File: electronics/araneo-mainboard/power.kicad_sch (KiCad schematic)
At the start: 1 part, among them IC3 TPS54302DDCR

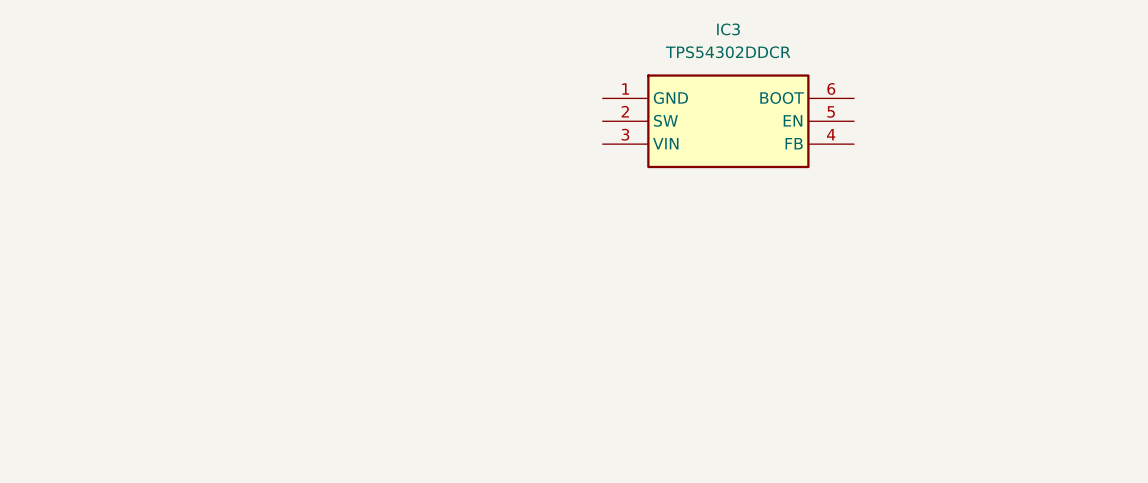
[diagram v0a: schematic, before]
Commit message: add components schematics
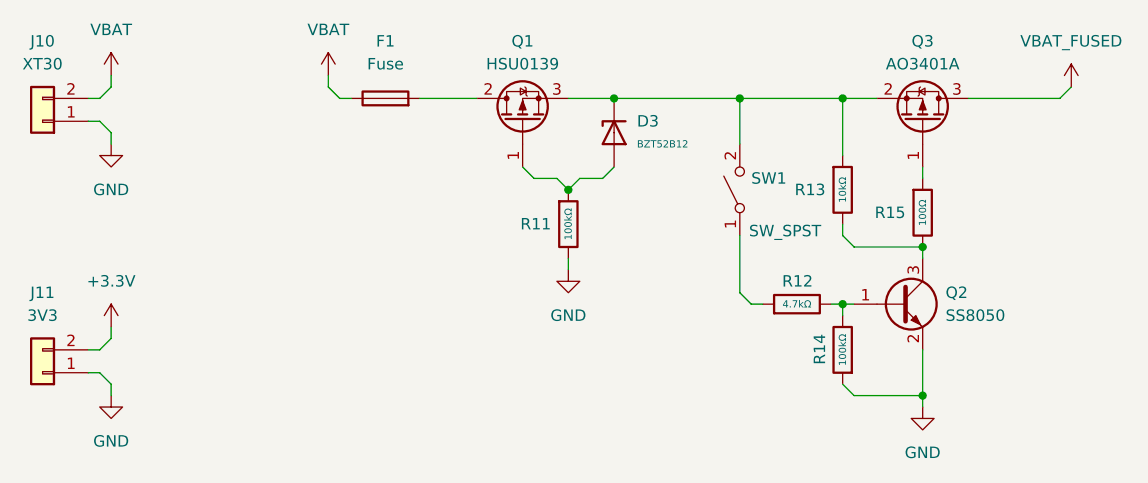
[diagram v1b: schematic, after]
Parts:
- removed IC3: TPS54302DDCR, SOT95P280X110-6N, symbol Symbols:TPS54302DDCR
- added D3: BZT52B12, PCM_JLCPCB:D_SOD-123, symbol PCM_JLCPCB-Diodes:Zener,BZT52B12
- added F1: Fuse, PCM_SparkFun-Fuse:Fuseholder_Automotive, symbol Device:Fuse
- added J10: XT30, Connector_AMASS:AMASS_XT30U-F_1x02_P5.0mm_Vertical, symbol Connector_Generic:Conn_01x02
- added J11: 3V3, Connector_PinHeader_2.54mm:PinHeader_1x02_P2.54mm_Vertical, symbol Connector_Generic:Conn_01x02
- added Q1: HSU0139, HSU0139:HSU0139, symbol Symbols:HSU0139
- added Q2: SS8050, Package_TO_SOT_SMD:SOT-23, symbol Transistor_BJT:SS8050
- added Q3: AO3401A, Package_TO_SOT_SMD:SOT-23, symbol Transistor_FET:AO3401A
- added R11, R14: 100kΩ, PCM_JLCPCB:R_0402, symbol PCM_JLCPCB-Resistors:0402,1.2kΩ
- added R12: 4.7kΩ, PCM_JLCPCB:R_0402, symbol PCM_JLCPCB-Resistors:0402,1.2kΩ
- added R13: 10kΩ, PCM_JLCPCB:R_0402, symbol PCM_JLCPCB-Resistors:0402,1.2kΩ
- added R15: 100Ω, PCM_JLCPCB:R_0402, symbol PCM_JLCPCB-Resistors:0402,1.2kΩ
- added SW1: SW_SPST, Button_Switch_THT:SW_NKK_GW12LJP, symbol Switch:SW_SPST
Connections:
- new net: Q3.1 (G), R15.1
- new net: D3.1, Q1.2 (S), Q1.3 (S), Q3.2 (S), R13.1, SW1.2 (B)
- new net: Q2.3 (C), R13.2, R15.2
- new net: Q2.1 (B), R12.2, R14.2
- new net: F1.2, Q1.2 (S)
- new net: D3.2, Q1.1 (G), R11.1
- new net: R12.1, SW1.1 (A)
- new net +3.3V: J11.2 (Pin_2)
- new net GND: J10.1 (Pin_1), J11.1 (Pin_1), Q2.2 (E), R11.2, R14.1
- new net VBAT: F1.1, J10.2 (Pin_2)
- new net VBAT_FUSED: Q3.3 (D)

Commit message: electronics: assign footprints
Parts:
- Q1: footprint HSU0139:HSU0139 -> Custom:HSU0139
- SW1: footprint Button_Switch_THT:SW_NKK_GW12LJP -> PCM_SparkFun-Connector:ScrewTerminal_1x02_P3.5mm_Blue
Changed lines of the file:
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@@
 			)
 		)
-		(property "Footprint" "Button_Switch_THT:SW_NKK_GW12LJP"
+		(property "Footprint" "PCM_SparkFun-Connector:ScrewTerminal_1x02_P3.5mm_Blue"
 			(at 146.05 72.39 0)
 			(hide yes)
@@
 			)
 		)
-		(property "Footprint" "HSU0139:HSU0139"
+		(property "Footprint" "Custom:HSU0139"
 			(at 123.825 59.69 0)
 			(hide yes)

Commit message: add first layout
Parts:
- removed Q1: HSU0139, Custom:HSU0139, symbol Symbols:HSU0139
- added Q4: DMP3056LSS-13, PCM_SparkFun-Semiconductor-Standard:SO-8, symbol Transistor_FET:AO3401A
- F1: footprint PCM_SparkFun-Fuse:Fuseholder_Automotive -> Custom:3568
- Q3: value AO3401A -> DMP3056LSS-13; footprint Package_TO_SOT_SMD:SOT-23 -> PCM_SparkFun-Semiconductor-Standard:SO-8
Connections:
- net VBAT_FUSED: now also Q3.5 (D), Q3.6 (D), Q3.7 (D), Q3.8 (D); no longer Q3.3 (D)
- net SW_1: now reaches Q3.1 (S)
- net SW_1: now also D3.1, Q3.2 (S), Q3.3 (S), R13.1, SW1.2 (B), Q4.1 (S), Q4.2 (S), Q4.3 (S); no longer R15.1
- net SW_C_R: now reaches Q2.3 (C), R13.2, R15.2
- net SW_B_PD: now reaches Q2.1 (B), R12.2, R14.2
- net VBAT_F: now reaches F1.2
- net VBAT_F: now also Q4.5 (D), Q4.6 (D), Q4.7 (D), Q4.8 (D)
- net POL_ZENER: now reaches D3.2, R11.1
- net POL_ZENER: now also Q4.4 (G)
- net SW_2: now reaches R12.1, SW1.1 (A)
- new net SW_G: Q3.4 (G), R15.1
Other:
- moved on the sheet: F1
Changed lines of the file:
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@@
 	(wire
 		(pts
-			(xy 110.49 62.23) (xy 116.84 62.23)
+			(xy 105.41 62.23) (xy 116.84 62.23)
 		)
 		(stroke
@@
 	(wire
 		(pts
-			(xy 100.33 60.96) (xy 101.6 62.23)
+			(xy 95.25 60.96) (xy 96.52 62.23)
 		)
 		(stroke
@@
 	(wire
 		(pts
-			(xy 101.6 62.23) (xy 102.87 62.23)
+			(xy 96.52 62.23) (xy 97.79 62.23)
 		)
 		(stroke
@@
 	(wire
 		(pts
-			(xy 100.33 59.69) (xy 100.33 60.96)
+			(xy 95.25 59.69) (xy 95.25 60.96)
 		)
 		(stroke
@@
 		)
 	)
+	(label "SW_2"
+		(at 146.05 80.01 180)
+		(effects
+			(font
+				(size 1.27 1.27)
+			)
+			(justify right bottom)
+		)
+	)
+	(label "SW_C_R"
+		(at 166.37 80.01 0)
+		(effects
+			(font
+				(size 1.27 1.27)
+			)
+			(justify left bottom)
+		)
+	)
+	(label "VBAT_F"
+		(at 106.68 62.23 0)
+		(effects
+			(font
+				(size 1.27 1.27)
+			)
+			(justify left bottom)
+		)
+	)
+	(label "POL_ZENER"
+		(at 130.81 71.12 0)
+		(effects
+			(font
+				(size 1.27 1.27)
+			)
+			(justify left bottom)
+		)
+	)
+	(label "SW_1"
+		(at 146.05 66.04 0)
+		(effects
+			(font
+				(size 1.27 1.27)
+			)
+			(justify left bottom)
+		)
+	)
+	(label "SW_G"
+		(at 166.37 69.85 0)
+		(effects
+			(font
+				(size 1.27 1.27)
+			)
+			(justify left bottom)
+		)
+	)
+	(label "SW_B_PD"
+		(at 157.48 85.09 90)
+		(effects
+			(font
+				(size 1.27 1.27)
+			)
+			(justify left bottom)
+		)
+	)
 	(symbol
 		(lib_id "Connector_Generic:Conn_01x02")
@@
 	)
 	(symbol
+		(lib_name "AO3401A_1")
 		(lib_id "Transistor_FET:AO3401A")
 		(at 166.37 64.77 270)
@@
 			)
 		)
-		(property "Value" "AO3401A"
+		(property "Value" "DMP3056LSS-13"
 			(at 166.37 58.42 90)
 			(show_name no)
@@
 			)
 		)
-		(property "Footprint" "Package_TO_SOT_SMD:SOT-23"
+		(property "Footprint" "PCM_SparkFun-Semiconductor-Standard:SO-8"
 			(at 164.465 59.69 0)
 			(hide yes)
@@
 			)
 		)
-		(property "Description" "-4.0A Id, -30V Vds, P-Channel MOSFET, SOT-23"
+		(property "Description" "-6.0A Id, -30V Vds, P-Channel MOSFET, SOT-23"
 			(at 166.37 64.77 0)
 			(hide yes)
@@
 			)
 		)
+		(pin "5"
+		)
+		(pin "4"
+		)
+		(pin "1"
+		)
 		(pin "2"
 		)
 		(pin "3"
 		)
-		(pin "1"
+		(pin "7"
+		)
+		(pin "8"
+		)
+		(pin "6"
 		)
 		(instances
@@
 	(symbol
 		(lib_id "Device:Fuse")
-		(at 106.68 62.23 90)
+		(at 101.6 62.23 90)
 		(unit 1)
 		(body_style 1)
@@
 		(fields_autoplaced yes)
 		(property "Reference" "F1"
-			(at 106.68 55.88 90)
+			(at 101.6 55.88 90)
 			(show_name no)
 			(do_not_autoplace no)
@@
 		)
 		(property "Value" "Fuse"
-			(at 106.68 58.42 90)
+			(at 101.6 58.42 90)
 			(show_name no)
 			(do_not_autoplace no)
@@
 			)
 		)
-		(property "Footprint" "PCM_SparkFun-Fuse:Fuseholder_Automotive"
-			(at 106.68 64.008 90)
+		(property "Footprint" "Custom:3568"
+			(at 101.6 64.008 90)
 			(hide yes)
 			(show_name no)
@@
 		)
 		(property "Datasheet" ""
-			(at 106.68 62.23 0)
+			(at 101.6 62.23 0)
 			(hide yes)
 			(show_name no)
@@
 		)
 		(property "Description" "Fuse"
-			(at 106.68 62.23 0)
+			(at 101.6 62.23 0)
 			(hide yes)
 			(show_name no)
@@
 	(symbol
 		(lib_id "power:+5V")
-		(at 100.33 59.69 0)
+		(at 95.25 59.69 0)
 		(unit 1)
 		(body_style 1)
@@
 		(fields_autoplaced yes)
 		(property "Reference" "#PWR054"
-			(at 100.33 63.5 0)
+			(at 95.25 63.5 0)
 			(hide yes)
 			(show_name no)
@@
 		)
 		(property "Value" "VBAT"
-			(at 100.33 54.61 0)
+			(at 95.25 54.61 0)
 			(show_name no)
 			(do_not_autoplace no)
@@
 		)
 		(property "Footprint" ""
-			(at 100.33 59.69 0)
+			(at 95.25 59.69 0)
 			(hide yes)
 			(show_name no)
@@
 		)
 		(property "Datasheet" ""
-			(at 100.33 59.69 0)
+			(at 95.25 59.69 0)
 			(hide yes)
 			(show_name no)
@@
 		)
 		(property "Description" "Power symbol creates a global label with name \"+5V\""
-			(at 100.33 59.69 0)
+			(at 95.25 59.69 0)
 			(hide yes)
 			(show_name no)
@@
 	)
 	(symbol
+		(lib_name "AO3401A_2")
+		(lib_id "Transistor_FET:AO3401A")
+		(at 121.92 64.77 90)
+		(unit 1)
+		(body_style 1)
+		(exclude_from_sim no)
+		(in_bom yes)
+		(on_board yes)
+		(in_pos_files yes)
+		(dnp no)
+		(property "Reference" "Q4"
+			(at 121.92 55.88 90)
+			(show_name no)
+			(do_not_autoplace no)
+			(effects
+				(font
+					(size 1.27 1.27)
+				)
+			)
+		)
+		(property "Value" "DMP3056LSS-13"
+			(at 121.92 58.42 90)
+			(show_name no)
+			(do_not_autoplace no)
+			(effects
+				(font
+					(size 1.27 1.27)
+				)
+			)
+		)
+		(property "Footprint" "PCM_SparkFun-Semiconductor-Standard:SO-8"
+			(at 123.825 59.69 0)
+			(hide yes)
+			(show_name no)
+			(do_not_autoplace no)
+			(effects
+				(font
+					(size 1.27 1.27)
+					(italic yes)
+				)
+				(justify left)
+			)
+		)
+		(property "Datasheet" "http://www.aosmd.com/pdfs/datasheet/AO3401A.pdf"
+			(at 125.73 59.69 0)
+			(hide yes)
+			(show_name no)
+			(do_not_autoplace no)
+			(effects
+				(font
+					(size 1.27 1.27)
+				)
+				(justify left)
+			)
+		)
+		(property "Description" "-6.0A Id, -30V Vds, P-Channel MOSFET, SOT-23"
+			(at 121.92 64.77 0)
+			(hide yes)
+			(show_name no)
+			(do_not_autoplace no)
+			(effects
+				(font
+					(size 1.27 1.27)
+				)
+			)
+		)
+		(pin "5"
+		)
+		(pin "4"
+		)
+		(pin "1"
+		)
+		(pin "2"
+		)
+		(pin "3"
+		)
+		(pin "7"
+		)
+		(pin "8"
+		)
+		(pin "6"
+		)
+		(instances
+			(project "araneo-mainboard"
+				(path "/f9fcb57c-0831-41d4-a374-fa7a29fb9e88/955d0e05-7aaa-4f45-8822-a7c91ddf7ad9"
+					(reference "Q4")
+					(unit 1)
+				)
+			)
+		)
+	)
+	(symbol
 		(lib_id "power:GND")
 		(at 127 81.28 0)
@@
 					(unit 1)
 				)
-			)
-		)
-	)
-	(symbol
-		(lib_id "Symbols:HSU0139")
-		(at 121.92 64.77 90)
-		(unit 1)
-		(body_style 1)
-		(exclude_from_sim no)
-		(in_bom yes)
-		(on_board yes)
-		(in_pos_files yes)
-		(dnp no)
-		(fields_autoplaced yes)
-		(property "Reference" "Q1"
-			(at 121.92 55.88 90)
-			(show_name no)
-			(do_not_autoplace no)
-			(effects
-				(font
-					(size 1.27 1.27)
-				)
-			)
-		)
-		(property "Value" "HSU0139"
-			(at 121.92 58.42 90)
-			(show_name no)
-			(do_not_autoplace no)
-			(effects
-				(font
-					(size 1.27 1.27)
-				)
-			)
-		)
-		(property "Footprint" "Custom:HSU0139"
-			(at 123.825 59.69 0)
-			(hide yes)
-			(show_name no)
-			(do_not_autoplace no)
-			(effects
-				(font
-					(size 1.27 1.27)
-				)
-				(justify left)
-			)
-		)
-		(property "Datasheet" "https://alltransistors.com/adv/pdfview.php?doc=hsu0139.pdf&dire=_huashuo"
-			(at 125.73 59.69 0)
-			(hide yes)
-			(show_name no)
-			(do_not_autoplace no)
-			(effects
-				(font
-					(size 1.27 1.27)
-				)
-				(justify left)
-			)
-		)
-		(property "Description" "-30A Id, -100V Vds, P-Channel MOSFET, TO-252-2"
-			(at 121.92 64.77 0)
-			(hide yes)
-			(show_name no)
-			(do_not_autoplace no)
-			(effects
-				(font
-					(size 1.27 1.27)
-				)
-			)
-		)
-		(pin "3"
-		)
-		(pin "2"
-		)
-		(pin "3"
-		)
-		(pin "1"
-		)
-		(pin "2"
-		)
-		(instances
-			(project "araneo-mainboard"
-				(path "/f9fcb57c-0831-41d4-a374-fa7a29fb9e88/955d0e05-7aaa-4f45-8822-a7c91ddf7ad9"
-					(reference "Q1")
-					(unit 1)
-				)

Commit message: electronics: update bom
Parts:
- F1, J10, J11, SW1: now left out of the parts list
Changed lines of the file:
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@@
 		(body_style 1)
 		(exclude_from_sim no)
-		(in_bom yes)
+		(in_bom no)
 		(on_board yes)
 		(in_pos_files yes)
@@
 		(body_style 1)
 		(exclude_from_sim no)
-		(in_bom yes)
+		(in_bom no)
 		(on_board yes)
 		(in_pos_files yes)
@@
 		(body_style 1)
 		(exclude_from_sim no)
-		(in_bom yes)
+		(in_bom no)
 		(on_board yes)
 		(in_pos_files yes)
@@
 		(body_style 1)
 		(exclude_from_sim no)
-		(in_bom yes)
+		(in_bom no)
 		(on_board yes)
 		(in_pos_files yes)

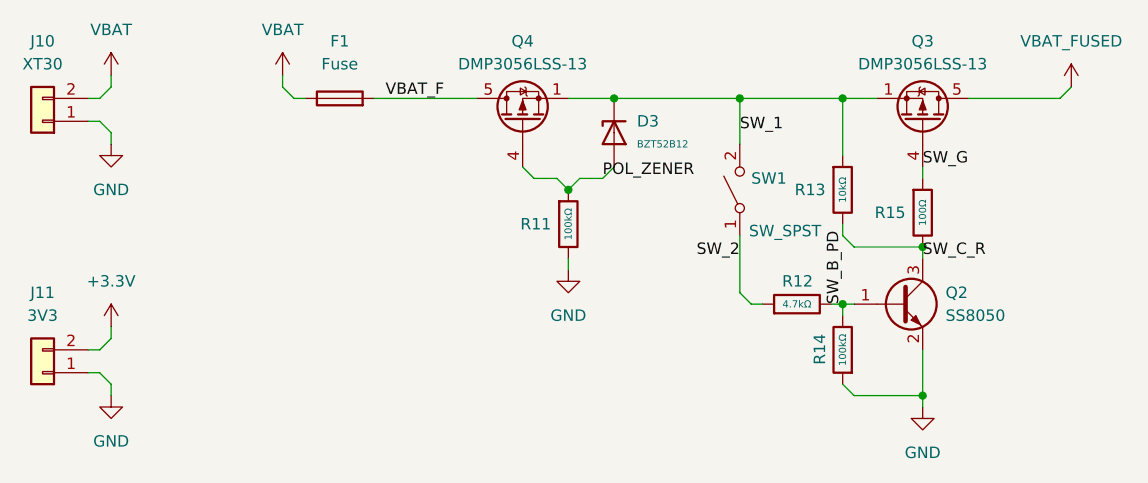
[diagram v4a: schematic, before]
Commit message: improve schematic and layout, add LCSC parts
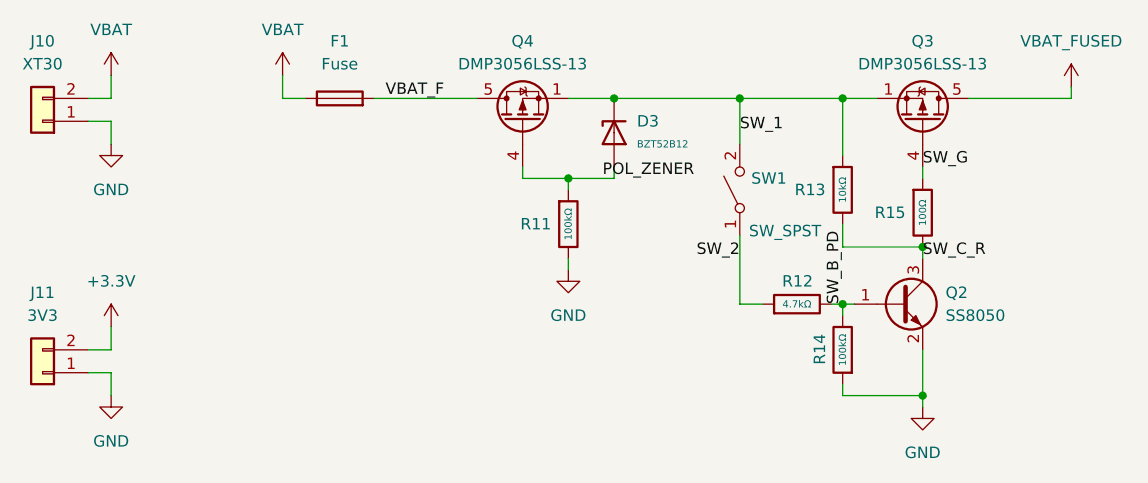
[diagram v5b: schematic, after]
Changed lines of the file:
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@@
 	(paper "A4")
 	(junction
+		(at 127 71.12)
+		(diameter 0)
+		(color 0 0 0 0)
+	)
+	(junction
 		(at 166.37 95.25)
 		(diameter 0)
@@
 	)
 	(junction
-		(at 127 72.39)
-		(diameter 0)
-		(color 0 0 0 0)
-	)
-	(junction
 		(at 146.05 62.23)
 		(diameter 0)
@@
 	(wire
 		(pts
-			(xy 146.05 83.82) (xy 147.32 85.09)
-		)
-		(stroke
-			(width 0)
-			(type default)
-		)
-	)
-	(wire
-		(pts
 			(xy 105.41 62.23) (xy 116.84 62.23)
 		)
@@
 	(wire
 		(pts
-			(xy 76.2 66.04) (xy 74.93 64.77)
-		)
-		(stroke
-			(width 0)
-			(type default)
-		)
-	)
-	(wire
-		(pts
-			(xy 76.2 60.96) (xy 74.93 62.23)
+			(xy 76.2 87.63) (xy 76.2 90.17)
+		)
+		(stroke
+			(width 0)
+			(type default)
+		)
+	)
+	(wire
+		(pts
+			(xy 146.05 85.09) (xy 148.59 85.09)
 		)
 		(stroke
@@
 	(wire
 		(pts
-			(xy 95.25 60.96) (xy 96.52 62.23)
-		)
-		(stroke
-			(width 0)
-			(type default)
-		)
-	)
-	(wire
-		(pts
 			(xy 166.37 69.85) (xy 166.37 71.12)
 		)
@@
 	(wire
 		(pts
-			(xy 128.27 71.12) (xy 130.81 71.12)
-		)
-		(stroke
-			(width 0)
-			(type default)
-		)
-	)
-	(wire
-		(pts
-			(xy 73.66 64.77) (xy 74.93 64.77)
+			(xy 95.25 62.23) (xy 97.79 62.23)
+		)
+		(stroke
+			(width 0)
+			(type default)
+		)
+	)
+	(wire
+		(pts
+			(xy 182.88 60.96) (xy 182.88 62.23)
+		)
+		(stroke
+			(width 0)
+			(type default)
+		)
+	)
+	(wire
+		(pts
+			(xy 73.66 64.77) (xy 76.2 64.77)
 		)
 		(stroke
@@
 	(wire
 		(pts
-			(xy 73.66 90.17) (xy 74.93 90.17)
+			(xy 73.66 90.17) (xy 76.2 90.17)
+		)
+		(stroke
+			(width 0)
+			(type default)
+		)
+	)
+	(wire
+		(pts
+			(xy 157.48 78.74) (xy 166.37 78.74)
 		)
 		(stroke
@@
 	(wire
 		(pts
-			(xy 76.2 87.63) (xy 76.2 88.9)
-		)
-		(stroke
-			(width 0)
-			(type default)
-		)
-	)
-	(wire
-		(pts
-			(xy 125.73 71.12) (xy 127 72.39)
-		)
-		(stroke
-			(width 0)
-			(type default)
-		)
-	)
-	(wire
-		(pts
 			(xy 157.48 62.23) (xy 157.48 68.58)
 		)
@@
 	(wire
 		(pts
-			(xy 128.27 71.12) (xy 127 72.39)
-		)
-		(stroke
-			(width 0)
-			(type default)
-		)
-	)
-	(wire
-		(pts
-			(xy 182.88 60.96) (xy 181.61 62.23)
-		)
-		(stroke
-			(width 0)
-			(type default)
-		)
-	)
-	(wire
-		(pts
-			(xy 158.75 78.74) (xy 166.37 78.74)
-		)
-		(stroke
-			(width 0)
-			(type default)
-		)
-	)
-	(wire
-		(pts
-			(xy 171.45 62.23) (xy 181.61 62.23)
-		)
-		(stroke
-			(width 0)
-			(type default)
-		)
-	)
-	(wire
-		(pts
-			(xy 157.48 76.2) (xy 157.48 77.47)
-		)
-		(stroke
-			(width 0)
-			(type default)
-		)
-	)
-	(wire
-		(pts
-			(xy 123.19 71.12) (xy 125.73 71.12)
-		)
-		(stroke
-			(width 0)
-			(type default)
-		)
-	)
-	(wire
-		(pts
-			(xy 157.48 93.98) (xy 158.75 95.25)
+			(xy 157.48 93.98) (xy 157.48 95.25)
+		)
+		(stroke
+			(width 0)
+			(type default)
+		)
+	)
+	(wire
+		(pts
+			(xy 171.45 62.23) (xy 182.88 62.23)
+		)
+		(stroke
+			(width 0)
+			(type default)
+		)
+	)
+	(wire
+		(pts
+			(xy 132.08 69.85) (xy 132.08 71.12)
+		)
+		(stroke
+			(width 0)
+			(type default)
+		)
+	)
+	(wire
+		(pts
+			(xy 76.2 59.69) (xy 76.2 62.23)
 		)
 		(stroke
@@
 	(wire
 		(pts
-			(xy 76.2 66.04) (xy 76.2 67.31)
-		)
-		(stroke
-			(width 0)
-			(type default)
-		)
-	)
-	(wire
-		(pts
-			(xy 76.2 59.69) (xy 76.2 60.96)
-		)
-		(stroke
-			(width 0)
-			(type default)
-		)
-	)
-	(wire
-		(pts
-			(xy 73.66 62.23) (xy 74.93 62.23)
+			(xy 127 71.12) (xy 127 72.39)
+		)
+		(stroke
+			(width 0)
+			(type default)
+		)
+	)
+	(wire
+		(pts
+			(xy 121.92 69.85) (xy 121.92 71.12)
+		)
+		(stroke
+			(width 0)
+			(type default)
+		)
+	)
+	(wire
+		(pts
+			(xy 76.2 64.77) (xy 76.2 67.31)
+		)
+		(stroke
+			(width 0)
+			(type default)
+		)
+	)
+	(wire
+		(pts
+			(xy 73.66 62.23) (xy 76.2 62.23)
+		)
+		(stroke
+			(width 0)
+			(type default)
+		)
+	)
+	(wire
+		(pts
+			(xy 127 71.12) (xy 132.08 71.12)
+		)
+		(stroke
+			(width 0)
+			(type default)
+		)
+	)
+	(wire
+		(pts
+			(xy 157.48 95.25) (xy 166.37 95.25)
+		)
+		(stroke
+			(width 0)
+			(type default)
+		)
+	)
+	(wire
+		(pts
+			(xy 121.92 71.12) (xy 127 71.12)
 		)
 		(stroke
@@
 	(wire
 		(pts
-			(xy 146.05 77.47) (xy 146.05 83.82)
-		)
-		(stroke
-			(width 0)
-			(type default)
-		)
-	)
-	(wire
-		(pts
-			(xy 76.2 93.98) (xy 74.93 92.71)
+			(xy 146.05 77.47) (xy 146.05 85.09)
 		)
 		(stroke
@@
 	(wire
 		(pts
-			(xy 157.48 77.47) (xy 158.75 78.74)
+			(xy 157.48 76.2) (xy 157.48 78.74)
 		)
 		(stroke
@@
 	(wire
 		(pts
-			(xy 158.75 95.25) (xy 166.37 95.25)
-		)
-		(stroke
-			(width 0)
-			(type default)
-		)
-	)
-	(wire
-		(pts
 			(xy 166.37 95.25) (xy 166.37 96.52)
 		)
@@
 	(wire
 		(pts
-			(xy 132.08 69.85) (xy 130.81 71.12)
-		)
-		(stroke
-			(width 0)
-			(type default)
-		)
-	)
-	(wire
-		(pts
-			(xy 76.2 93.98) (xy 76.2 95.25)
-		)
-		(stroke
-			(width 0)
-			(type default)
-		)
-	)
-	(wire
-		(pts
 			(xy 157.48 85.09) (xy 157.48 86.36)
 		)
@@
 	(wire
 		(pts
-			(xy 76.2 88.9) (xy 74.93 90.17)
-		)
-		(stroke
-			(width 0)
-			(type default)
-		)
-	)
-	(wire
-		(pts
-			(xy 96.52 62.23) (xy 97.79 62.23)
-		)
-		(stroke
-			(width 0)
-			(type default)
-		)
-	)
-	(wire
-		(pts
-			(xy 73.66 92.71) (xy 74.93 92.71)
-		)
-		(stroke
-			(width 0)
-			(type default)
-		)
-	)
-	(wire
-		(pts
-			(xy 121.92 69.85) (xy 123.19 71.12)
-		)
-		(stroke
-			(width 0)
-			(type default)
-		)
-	)
-	(wire
-		(pts
-			(xy 95.25 59.69) (xy 95.25 60.96)
-		)
-		(stroke
-			(width 0)
-			(type default)
-		)
-	)
-	(wire
-		(pts
-			(xy 147.32 85.09) (xy 148.59 85.09)
-		)
-		(stroke
+			(xy 76.2 92.71) (xy 76.2 95.25)
+		)
+		(stroke
+			(width 0)
+			(type default)
+		)
+	)
+	(wire
+		(pts
+			(xy 73.66 92.71) (xy 76.2 92.71)
+		)
+		(stroke
+			(width 0)
+			(type default)
+		)
+	)
+	(wire
+		(pts
+			(xy 95.25 59.69) (xy 95.25 62.23)
+		)
+		(stroke
